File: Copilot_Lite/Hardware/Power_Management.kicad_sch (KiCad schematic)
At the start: 21 parts, among them J1 POWER_MODES, Q1 BSS138, Q2 BUK7M27-80EX, Q3 BUK7M27-80EX, Q4 BSS138, U1 LM74502, U2 LM74502

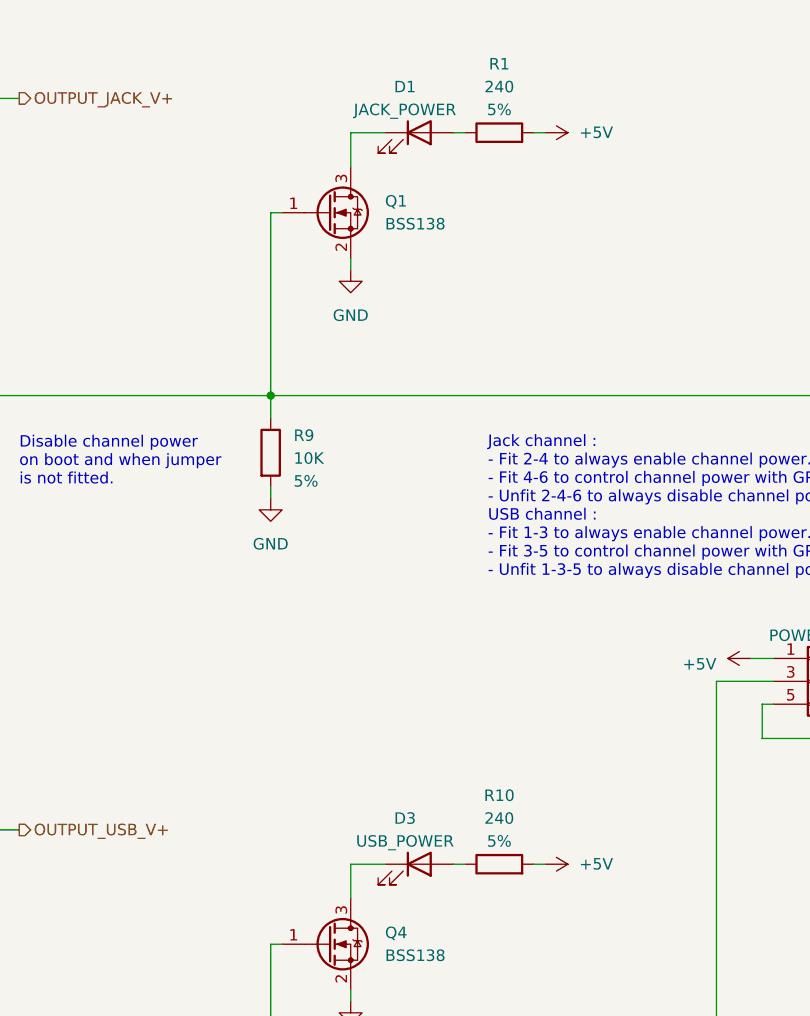
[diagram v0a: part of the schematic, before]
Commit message: Copilot_Lite: Hardware: Convert the schematic and the PCB to KiCad 9
Use the most recent files format, so any future board modification can be
more easily compared with the previous ones.

Signed-off-by: Adrien Ricciardi <aricciardi@baylibre.com>
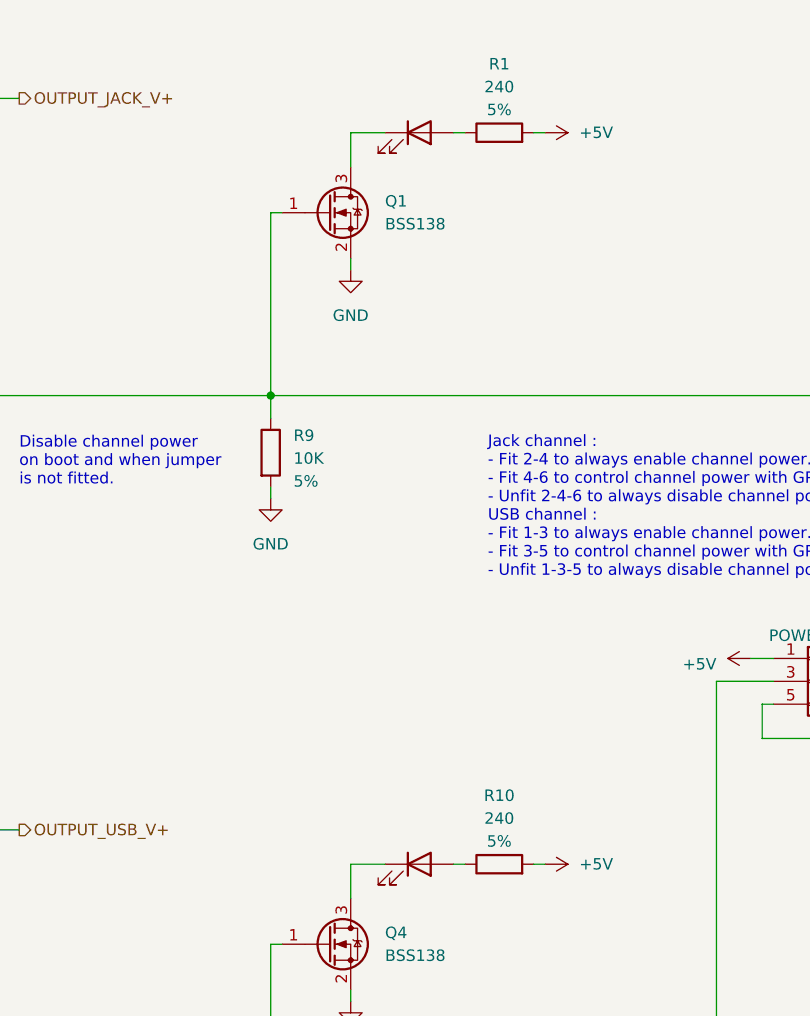
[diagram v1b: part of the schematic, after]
